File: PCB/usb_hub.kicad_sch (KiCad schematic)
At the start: 23 parts, among them J1 918-418K2023S40001, J2 901-211A1021D10100, J3 901-211A1021D10100, U1 GL852G-OHY60, Y1 CO22H4-12.000-WPGDTSNL

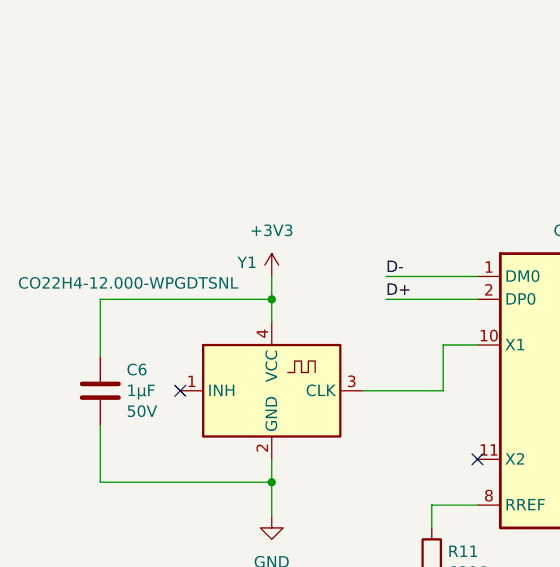
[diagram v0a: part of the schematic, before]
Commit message: Add the USB to JTAG bridge
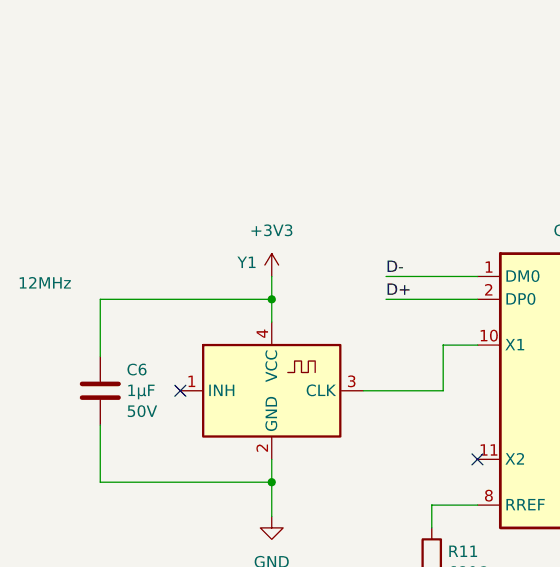
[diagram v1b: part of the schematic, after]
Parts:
- U1: LCSC (none) -> C7501404; Part_number (none) -> GL852G-OHY60
- Y1: value CO22H4-12.000-WPGDTSNL -> 12MHz; footprint Oscillator:Oscillator_SMD_Kyocera_KC2520Z-4Pin_2.5x2.0mm -> Crystal:Crystal_SMD_2520-4Pin_2.5x2.0mm
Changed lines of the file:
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@@
 			)
 		)
+		(property "LCSC" "C7501404"
+			(at 222.25 57.15 0)
+			(effects
+				(font
+					(size 1.27 1.27)
+				)
+				(hide yes)
+			)
+		)
+		(property "Part_number" "GL852G-OHY60"
+			(at 222.25 57.15 0)
+			(effects
+				(font
+					(size 1.27 1.27)
+				)
+				(hide yes)
+			)
+		)
 		(pin "8"
 		)
@@
 			)
 		)
+		(property "LCSC" "C7501404"
+			(at 101.6 153.67 0)
+			(effects
+				(font
+					(size 1.27 1.27)
+				)
+				(hide yes)
+			)
+		)
+		(property "Part_number" "GL852G-OHY60"
+			(at 101.6 153.67 0)
+			(effects
+				(font
+					(size 1.27 1.27)
+				)
+				(hide yes)
+			)
+		)
 		(pin "29"
 		)
@@
 			)
 		)
+		(property "LCSC" "C7501404"
+			(at 177.8 55.88 0)
+			(effects
+				(font
+					(size 1.27 1.27)
+				)
+				(hide yes)
+			)
+		)
+		(property "Part_number" "GL852G-OHY60"
+			(at 177.8 55.88 0)
+			(effects
+				(font
+					(size 1.27 1.27)
+				)
+				(hide yes)
+			)
+		)
 		(pin "22"
 		)
@@
 			)
 		)
+		(property "LCSC" "C7501404"
+			(at 222.25 31.75 0)
+			(effects
+				(font
+					(size 1.27 1.27)
+				)
+				(hide yes)
+			)
+		)
+		(property "Part_number" "GL852G-OHY60"
+			(at 222.25 31.75 0)
+			(effects
+				(font
+					(size 1.27 1.27)
+				)
+				(hide yes)
+			)
+		)
 		(pin "8"
 		)
@@
 			)
 		)
-		(property "Value" "CO22H4-12.000-WPGDTSNL"
+		(property "Value" "12MHz"
 			(at 35.306 140.462 0)
 			(effects
@@
 			)
 		)
-		(property "Footprint" "Oscillator:Oscillator_SMD_Kyocera_KC2520Z-4Pin_2.5x2.0mm"
+		(property "Footprint" "Crystal:Crystal_SMD_2520-4Pin_2.5x2.0mm"
 			(at 67.31 148.59 0)
 			(effects
@@
 			)
 		)
+		(property "LCSC" "C7501404"
+			(at 222.25 133.35 0)
+			(effects
+				(font
+					(size 1.27 1.27)
+				)
+				(hide yes)
+			)
+		)
+		(property "Part_number" "GL852G-OHY60"
+			(at 222.25 133.35 0)
+			(effects
+				(font
+					(size 1.27 1.27)
+				)
+				(hide yes)
+			)
+		)
 		(pin "15"
 		)
@@
 			(effects
 				(font
+					(size 1.27 1.27)
+				)
+				(hide yes)
+			)
+		)
+		(property "LCSC" "C7501404"
+			(at 222.25 95.25 0)
+			(effects
+				(font
+					(size 1.27 1.27)
+				)
+				(hide yes)
+			)
+		)
+		(property "Part_number" "GL852G-OHY60"
+			(at 222.25 95.25 0)
+			(effects
+				(font

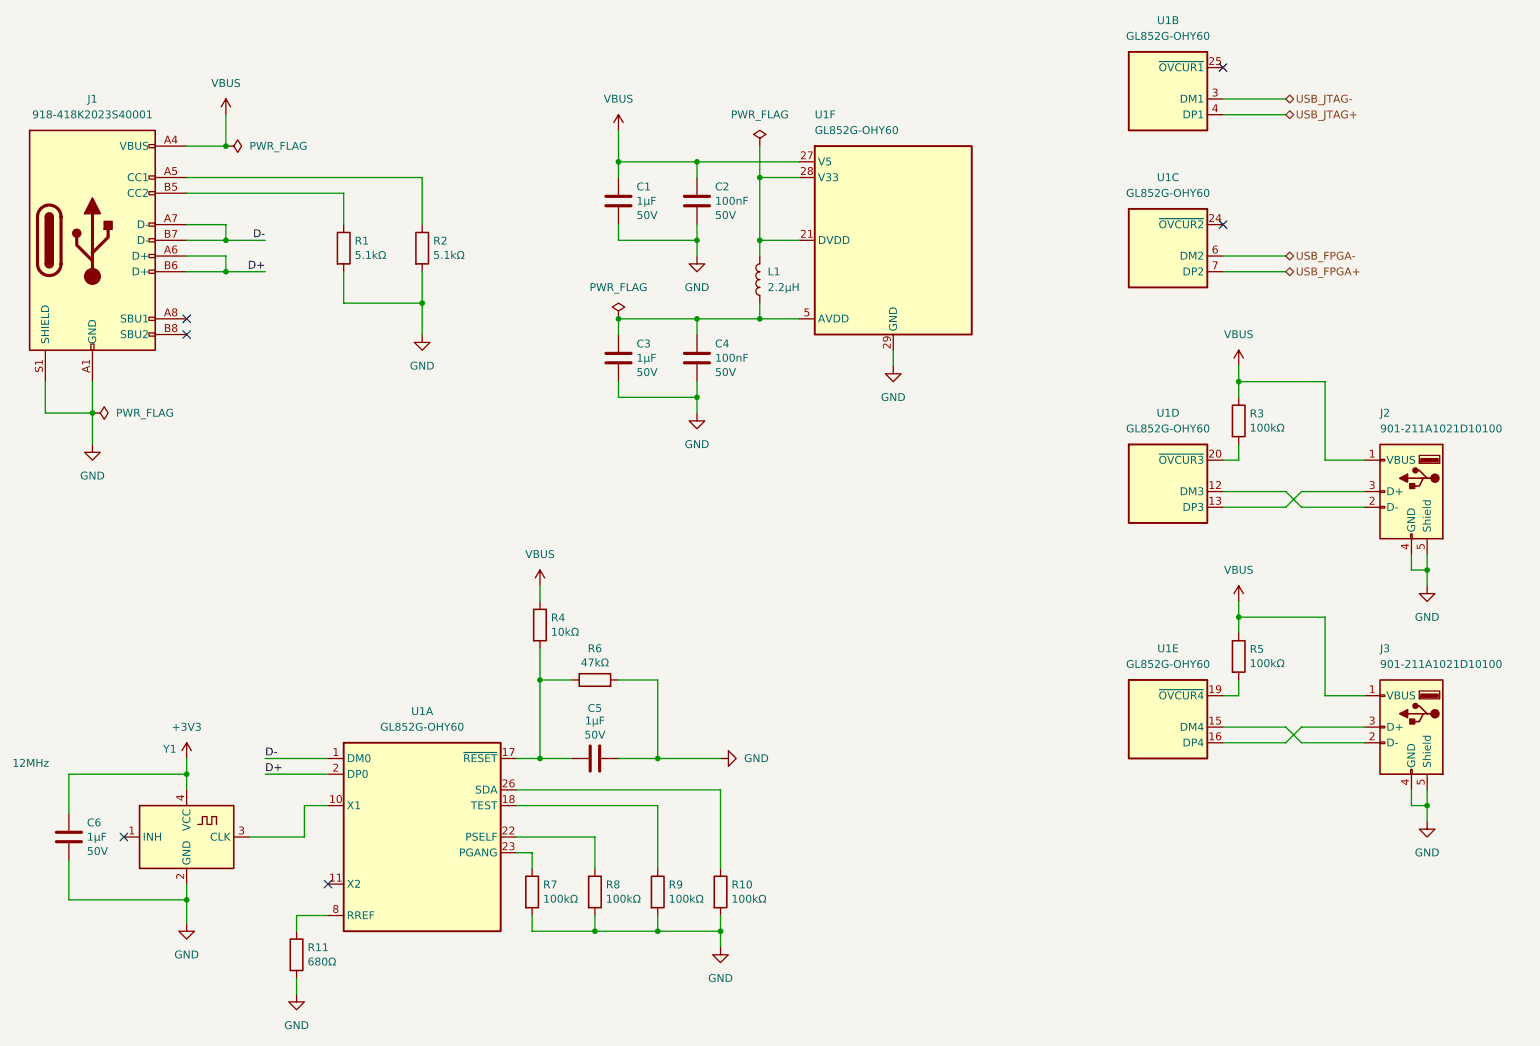
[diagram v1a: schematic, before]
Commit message: Improve the CH347F schematics and added 3D models
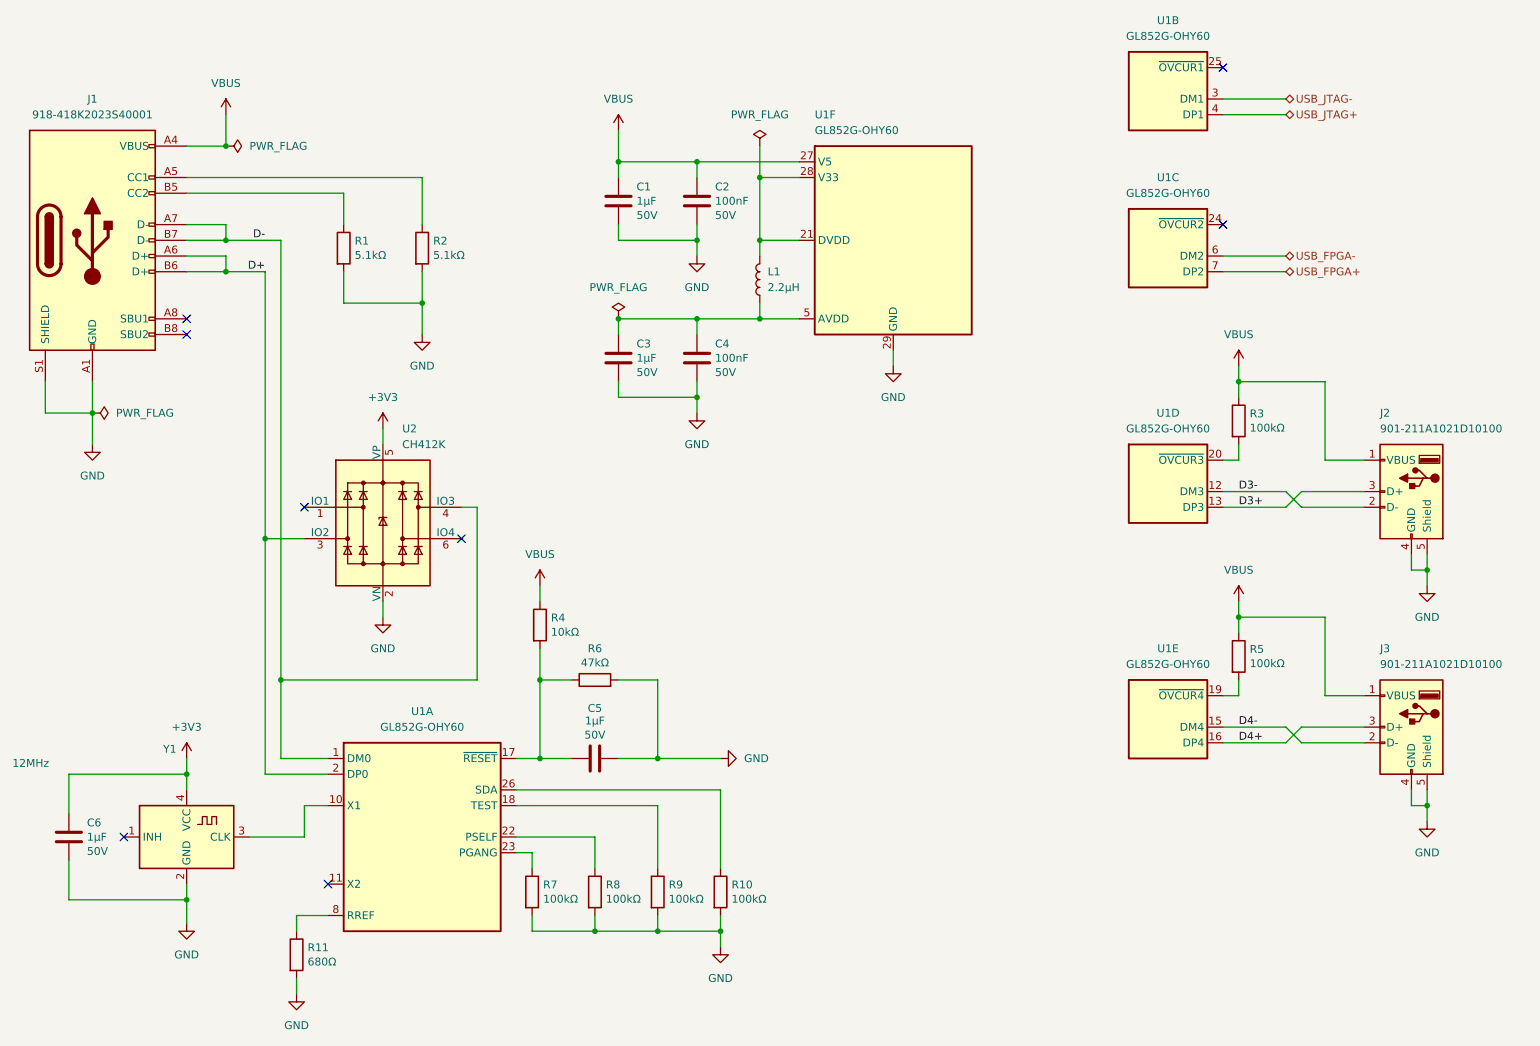
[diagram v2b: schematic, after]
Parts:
- added U2: CH412K, Package_TO_SOT_SMD:SOT-363_SC-70-6, symbol clavier:CH412K
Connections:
- net +3V3: now also U2.5 (VP)
- net D+: now also U2.3 (IO2)
- net D-: now also U2.4 (IO3)
- net GND: now also U2.2 (VN)
- net D3-: now reaches J2.2 (D-), U1.12 (DM3)
- net D3+: now reaches J2.3 (D+), U1.13 (DP3)
- net D4-: now reaches J3.2 (D-), U1.15 (DM4)
- net D4+: now reaches J3.3 (D+), U1.16 (DP4)
- no-connect marks 6 -> 8

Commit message: Add LICENSE and minor improvements
- Filled the title blocks
- Connected the LEDs to the FPGA
- Changed the FPGA programming header
- Added USB fuse and capacitors
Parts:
- added C5, C7: 22µF, Capacitor_SMD:C_0805_2012Metric, symbol Device:C
- added F1: Polyfuse, Fuse:Fuse_0805_2012Metric_Pad1.15x1.40mm_HandSolder, symbol Device:Polyfuse
- renumbered C5 to C6, C6 to C8, R6 to R5, R5 to R6
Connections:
- net GND: now also C5.2, C7.2
- net VBUS: now also C5.1, C7.1, F1.2; no longer J1.A4 (VBUS), J1.A9 (VBUS), J1.B4 (VBUS), J1.B9 (VBUS)
- new net: F1.1, J1.A4 (VBUS), J1.A9 (VBUS), J1.B4 (VBUS), J1.B9 (VBUS)
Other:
- company: (none) -> Copyright (c) 2025 L. Sartory
- title: (none) -> Clavier - USB hub
- moved on the sheet: J2, J3, R3, R6, U1D, U1E

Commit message: Place and route peripheral components
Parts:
- added C10, C7: 22µF, Capacitor_SMD:C_0805_2012Metric, symbol Device:C
- added C3: 1µF, Capacitor_SMD:C_0402_1005Metric_Pad0.74x0.62mm_HandSolder, symbol Device:C
- renumbered C8 to C11, C3 to C4, C4 to C5, C5 to C6, C6 to C8, C7 to C9
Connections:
- net D+: now also U2.1 (IO1); no longer U2.3 (IO2)
- net D3+: now also U1.7 (DP2); no longer U1.13 (DP3)
- net D3-: now also U1.6 (DM2); no longer U1.12 (DM3)
- net GND: now also C10.2, C3.2, C7.2
- net USB_FPGA+: now also U1.4 (DP1); no longer U1.7 (DP2)
- net USB_FPGA-: now also U1.3 (DM1); no longer U1.6 (DM2)
- net USB_JTAG+: now also U1.13 (DP3); no longer U1.4 (DP1)
- net USB_JTAG-: now also U1.12 (DM3); no longer U1.3 (DM1)
- net VBUS: now also C10.1, C7.1
- net at U1.24 (~{OVCUR2}): now also R3.2
- net at L1.2, U1.21 (DVDD), U1.28 (V33): now also C3.1
- net at U1.20 (~{OVCUR3}): no longer R3.2
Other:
- moved on the sheet: C1, C2, C6, C9, J2, J3, R3, R6, U1B, U1C, U1D, U1E

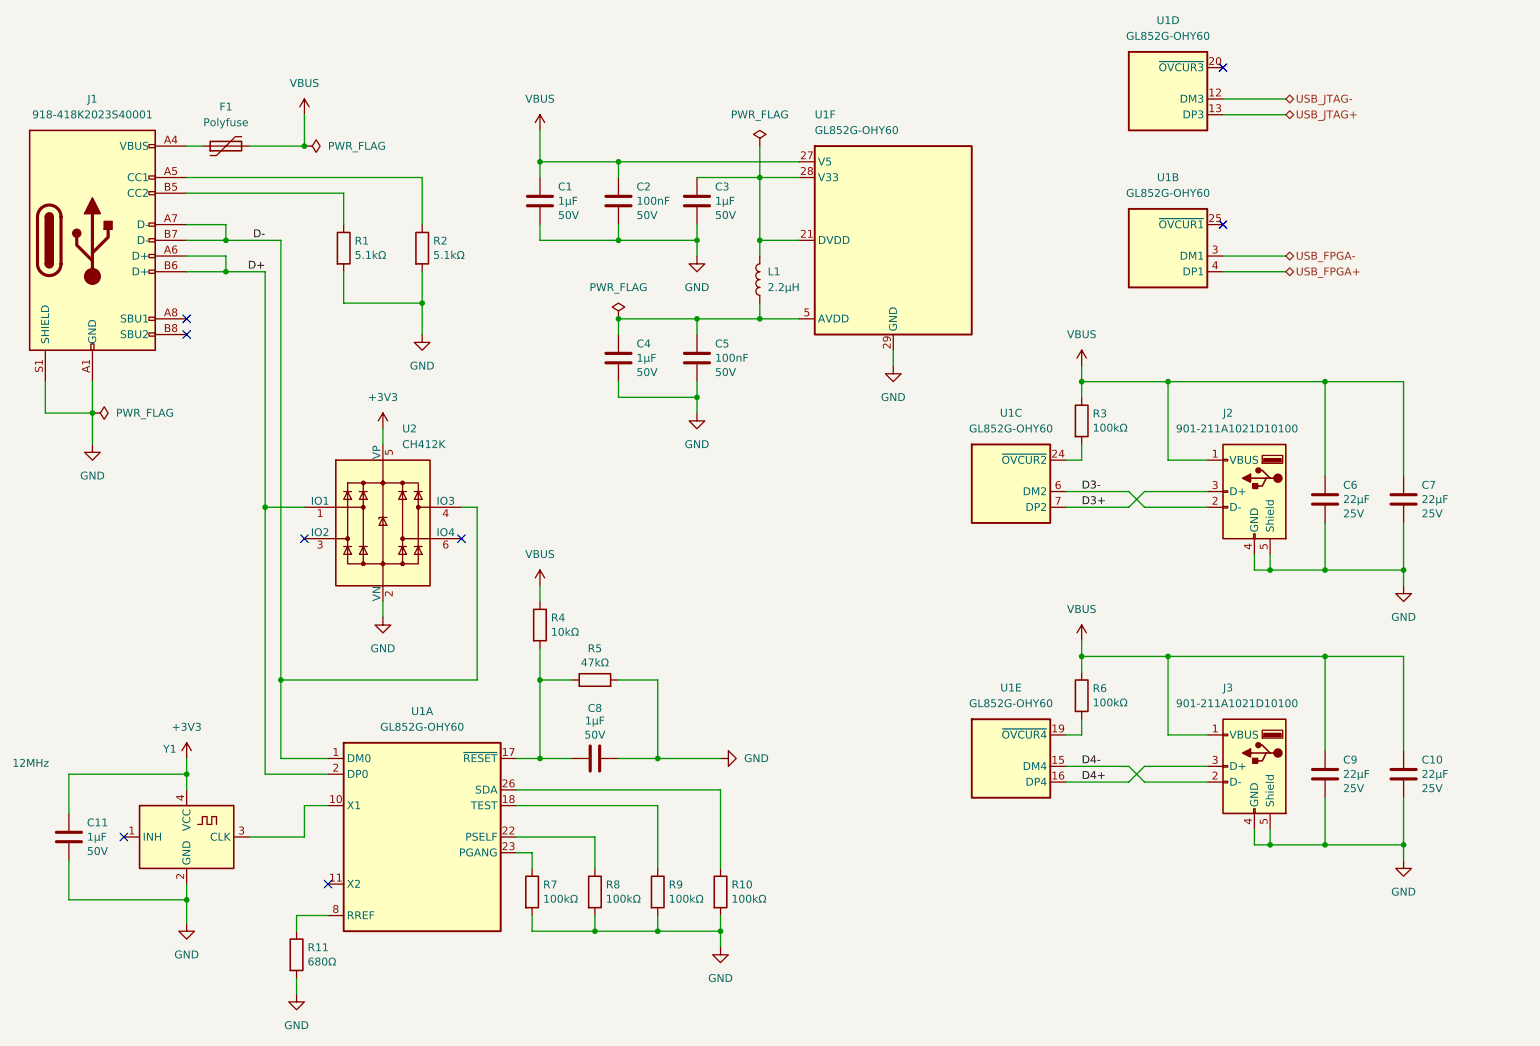
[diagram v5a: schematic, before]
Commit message: Add ESD protection
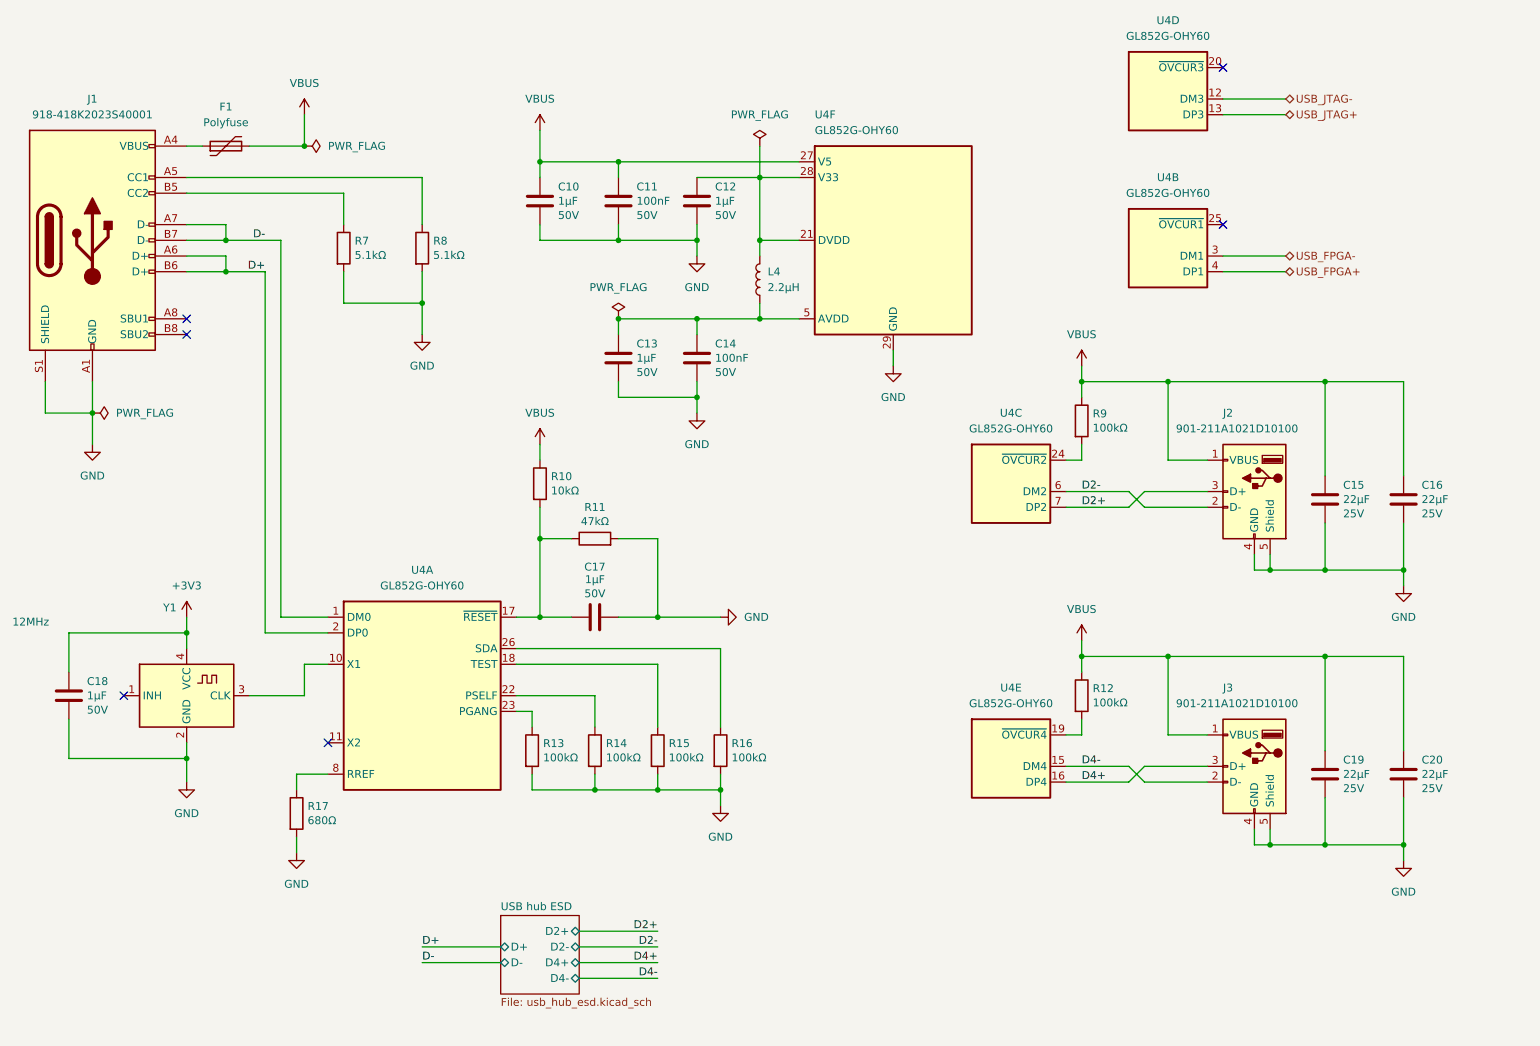
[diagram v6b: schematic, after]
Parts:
- removed U2: CH412K, Package_TO_SOT_SMD:SOT-363_SC-70-6, symbol clavier:CH412K
- renumbered C1 to C10, C2 to C11, C3 to C12, C4 to C13, C5 to C14, C6 to C15, C7 to C16, C8 to C17, C11 to C18, C9 to C19, C10 to C20, L1 to L4, R4 to R10, R5 to R11, R6 to R12, R7 to R13, R8 to R14, R9 to R15, R10 to R16, R11 to R17, R1 to R7, R2 to R8, R3 to R9, U1 to U4
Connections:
- net D3+ renamed D2+
- net D3- renamed D2-
- no-connect marks 8 -> 6
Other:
- added sheet USB hub ESD (usb_hub_esd.kicad_sch)
- moved on the sheet: C17, C18, R10, R11, R13, R14, R15, R16, R17, U4A, Y1
